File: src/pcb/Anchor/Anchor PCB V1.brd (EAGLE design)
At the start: 100.1 x 68.7 mm, 89 parts, among them IC1 ENC28J60-I_SS, IC2 TPS23750PWP, IC3 MIC5219-3.3YM5-TR, IC4 DWM1000, J1 0826-1X1T-GJ-F, J2 105017-0001, Q1 32 MHz, Q2 SUD06N10-225L, U1 ATSAMD21G-A, Y1 25 MHz

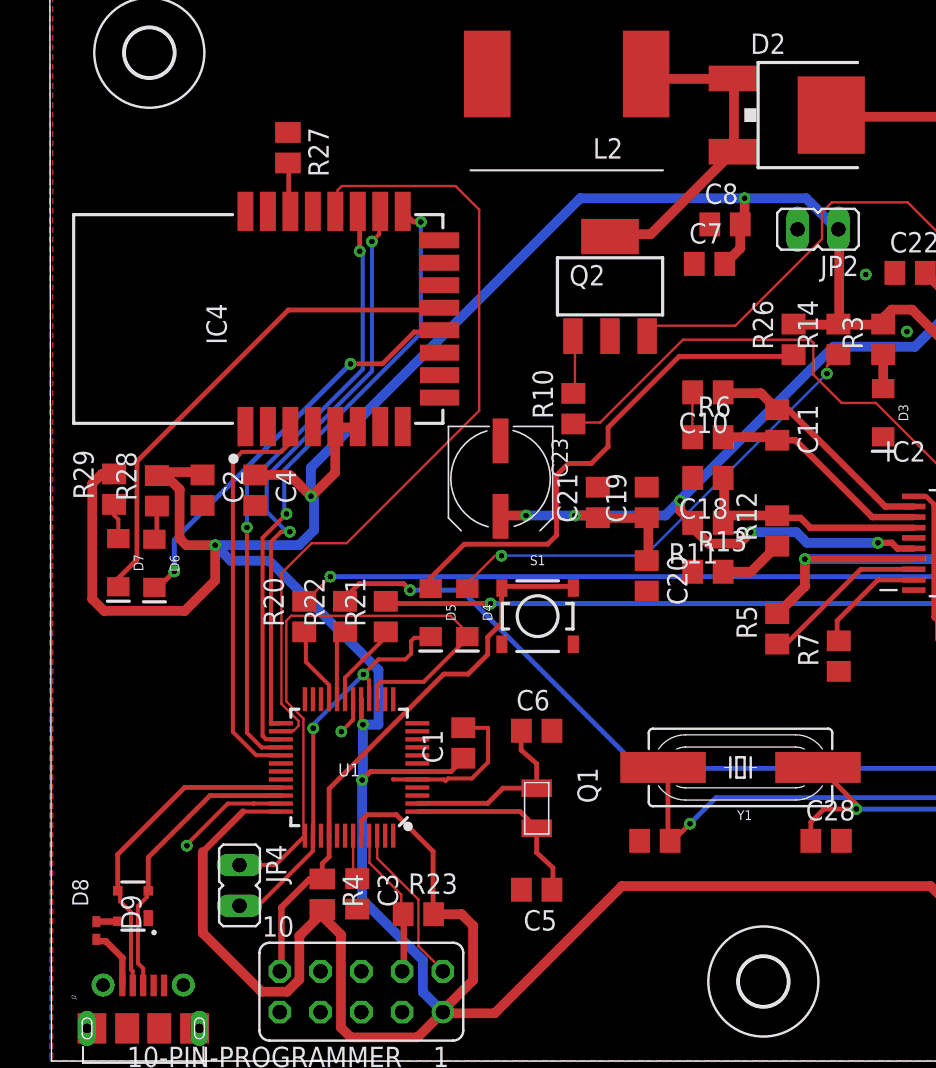
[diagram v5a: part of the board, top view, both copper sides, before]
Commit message: Rewiring and optimizing pcb layout
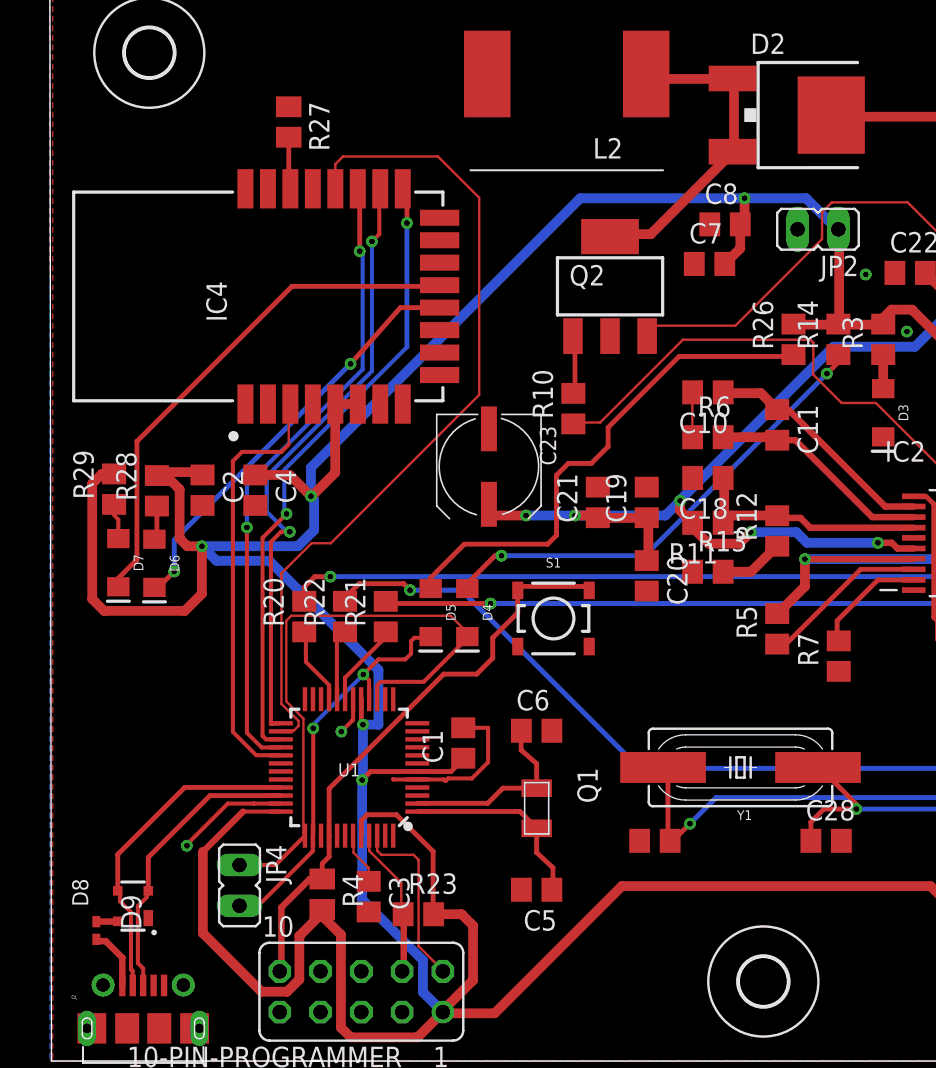
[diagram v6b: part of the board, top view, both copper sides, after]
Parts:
- moved R27 1.60 mm to (14.8, 58.5)
- moved IC4 1.40 mm to (24.4, 47.6)
- moved C23 1.04 mm to (27.3, 37.0)
- moved S1 1.00 mm to (31.3, 27.6)
- moved C3 0.73 mm to (19.8, 10.2)
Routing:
- net VCC: track 336.6 -> 338.5 mm
- net GND: track 43.8 -> 42.0 mm
- net RST_DWM: track 25.5 -> 27.0 mm
- net MOSI2_MC: track 37.0 -> 38.4 mm
- net MISO2_MC: track 38.1 -> 39.5 mm
- net RXLED_DWM: track 31.1 -> 32.4 mm
- net 5V: track 114.1 -> 115.4 mm
- net SWDIO: track 10.1 -> 11.3 mm
- net SCK2_MC: track 51.2 -> 52.1 mm
- net RESET: track 35.5 -> 36.5 mm
- net TXLED_DWM: track 25.6 -> 26.3 mm
- net SO_ETH: track 61.9 -> 62.4 mm

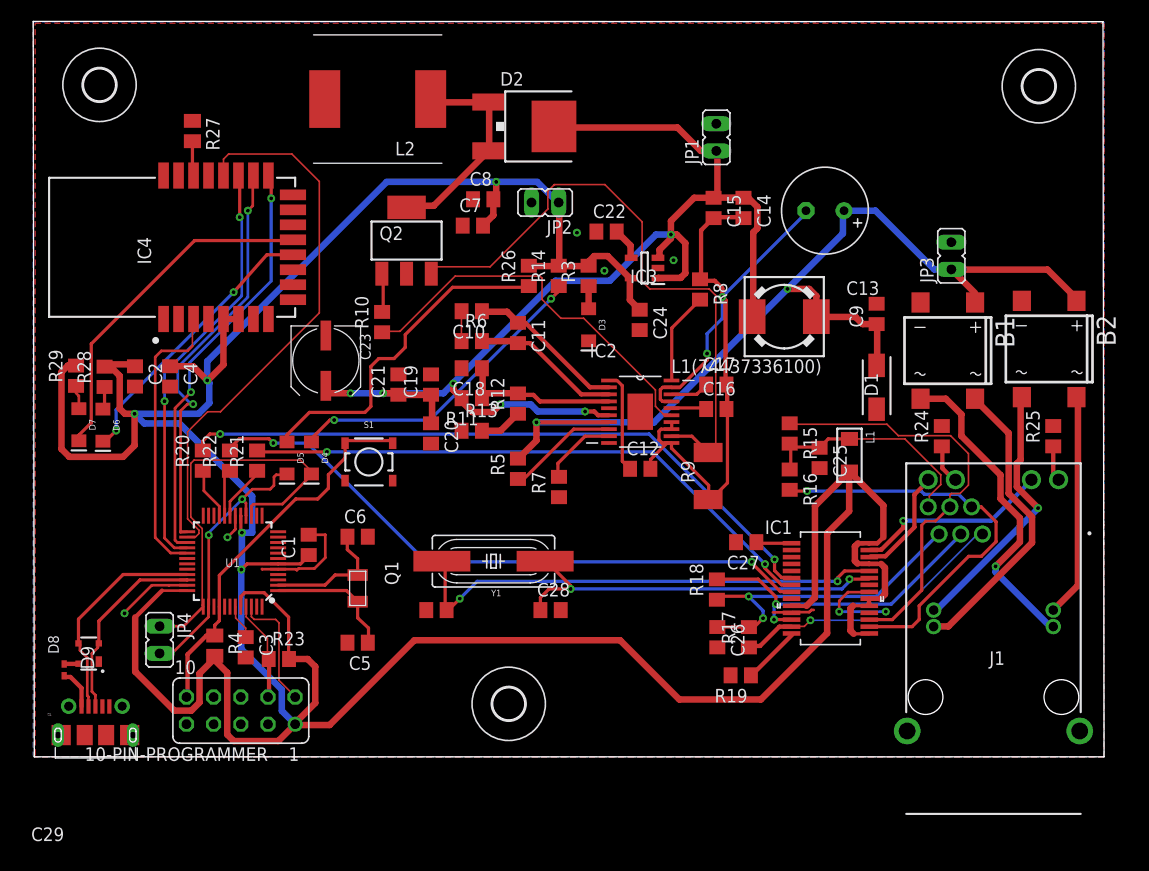
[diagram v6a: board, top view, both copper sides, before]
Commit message: Added backups for schematic and board
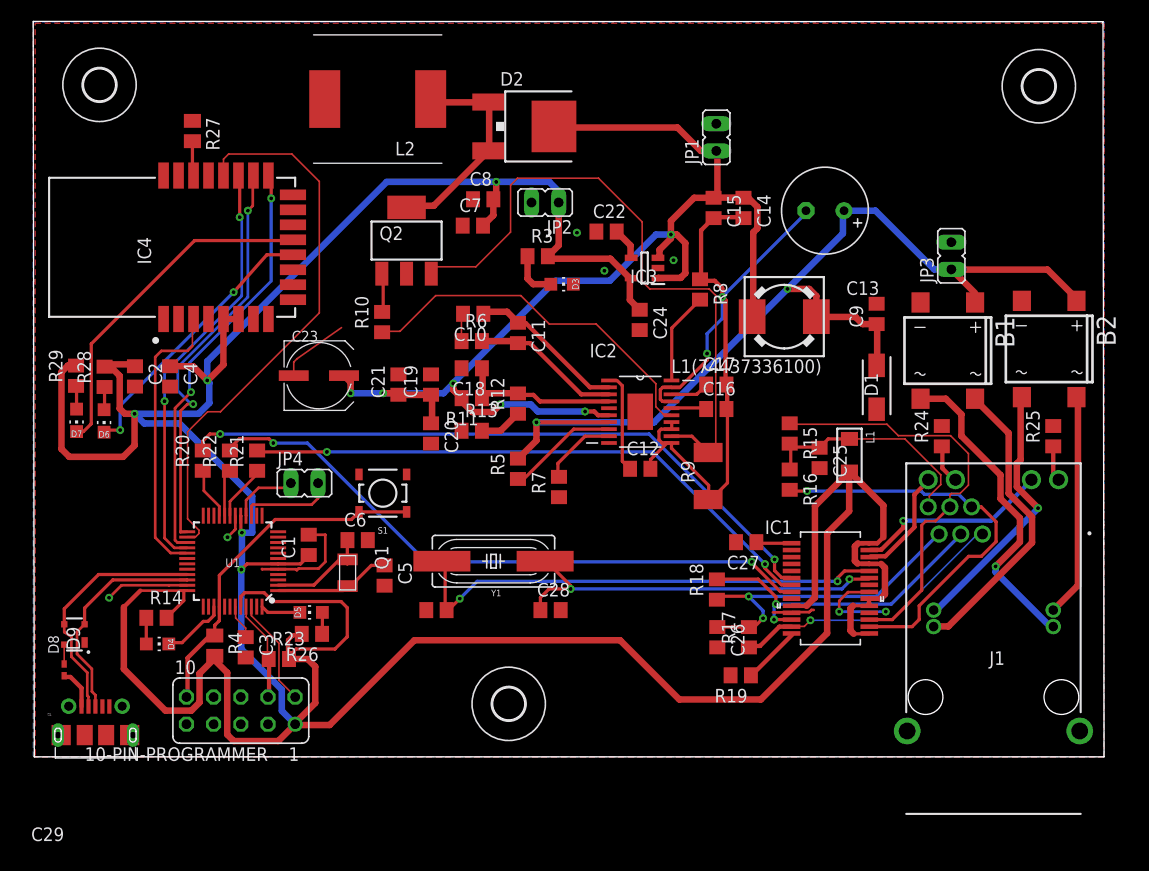
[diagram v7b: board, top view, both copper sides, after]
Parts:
- D3, D4, D5, D6, D7: device SparkFun-LED:LED-1206 -> led:CHIP-LED0805
- moved R14 49.4 mm to (11.4, 13.0), turned to 0 degrees
- moved R26 39.1 mm to (26.0, 11.5), turned to 180 degrees
- moved D4 22.6 mm to (11.5, 10.6)
- moved JP4 19.9 mm to (25.3, 25.6), turned to 270 degrees
- moved D5 14.6 mm to (25.9, 13.5), turned to 90 degrees
- moved C5 6.76 mm to (32.7, 16.9), turned to 270 degrees
- moved R3 5.10 mm to (47.1, 46.8), turned to 0 degrees
- moved D3 4.53 mm to (49.3, 44.2)
- moved S1 3.20 mm to (32.6, 24.6), turned to 180 degrees
- moved D9 2.23 mm to (3.75, 11.4)
- moved Q1 1.74 mm to (29.3, 17.2)
- moved C23 1.54 mm to (26.6, 35.6), turned to 0 degrees
- moved D7 0.46 mm to (3.95, 31.5), turned to 180 degrees
- moved D6 0.41 mm to (6.53, 31.4), turned to 180 degrees
- moved C6 0.31 mm to (30.2, 20.3)
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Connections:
- new net RXLED_MC: D5.C, U1.48
- new net TXLED_MC: D4.C, U1.39
- net RX_MC: now also JP4.1; no longer D5.C, JP4.2, U1.38
- net TX_MC: now also JP4.2; no longer D4.C, JP4.1, U1.37
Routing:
- net TX_MC: track 39.6 -> 8.87 mm
- net N$12: track 31.9 -> 2.04 mm
- net N$11: track 29.6 -> 2.45 mm, vias 2 -> 0
- net RX_MC: track 25.7 -> 6.30 mm, vias 2 -> 0
- net VCC: track 338.5 -> 355.5 mm
- net GND: track 42.0 -> 49.1 mm
- net TXLED_MC: track 0.00 -> 6.40 mm
- net RXLED_MC: track 0.00 -> 3.92 mm
- net RESET: track 36.5 -> 32.9 mm
- net USB+: track 18.2 -> 20.9 mm
- net USB-: track 20.7 -> 23.2 mm
- net N$9: track 2.12 -> 4.48 mm
- net GATE: track 36.7 -> 34.4 mm
- net RSP: track 57.7 -> 59.8 mm
- net XTAL2: track 11.9 -> 10.2 mm
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
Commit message: Solving connection problems
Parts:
- moved C2 9.25 mm to (18.6, 36.4)
- moved D7 2.42 mm to (6.36, 31.7)
- moved R29 2.42 mm to (6.31, 35.9)
- moved D6 2.42 mm to (8.93, 31.7)
- moved R28 2.42 mm to (8.97, 35.8)
- moved C23 0.90 mm to (27.5, 35.8)
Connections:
- net MISO2_MC renamed MISO2_DWM
- net MOSI2_MC renamed MOSI2_DWM
- net SCK2_MC renamed SCK2_DWM
- net GND: now also D6.C, D7.C
- net IRQ: now also U1.30
- net RXLED_DWM: now also R29.2; no longer D7.C
- net TXLED_DWM: now also R28.2; no longer D6.C
- net VCC: no longer R28.2, R29.2
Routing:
- net IRQ: track 3.25 -> 49.4 mm
- net VCC: track 355.5 -> 319.0 mm, vias 5 -> 4
- net RXLED_DWM: track 32.0 -> 23.7 mm
- net TXLED_DWM: track 26.0 -> 19.9 mm
- net GND: track 49.1 -> 48.5 mm
- net SCK2_DWM: track 52.1 -> 52.7 mm
